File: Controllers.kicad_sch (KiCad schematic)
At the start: 5 parts

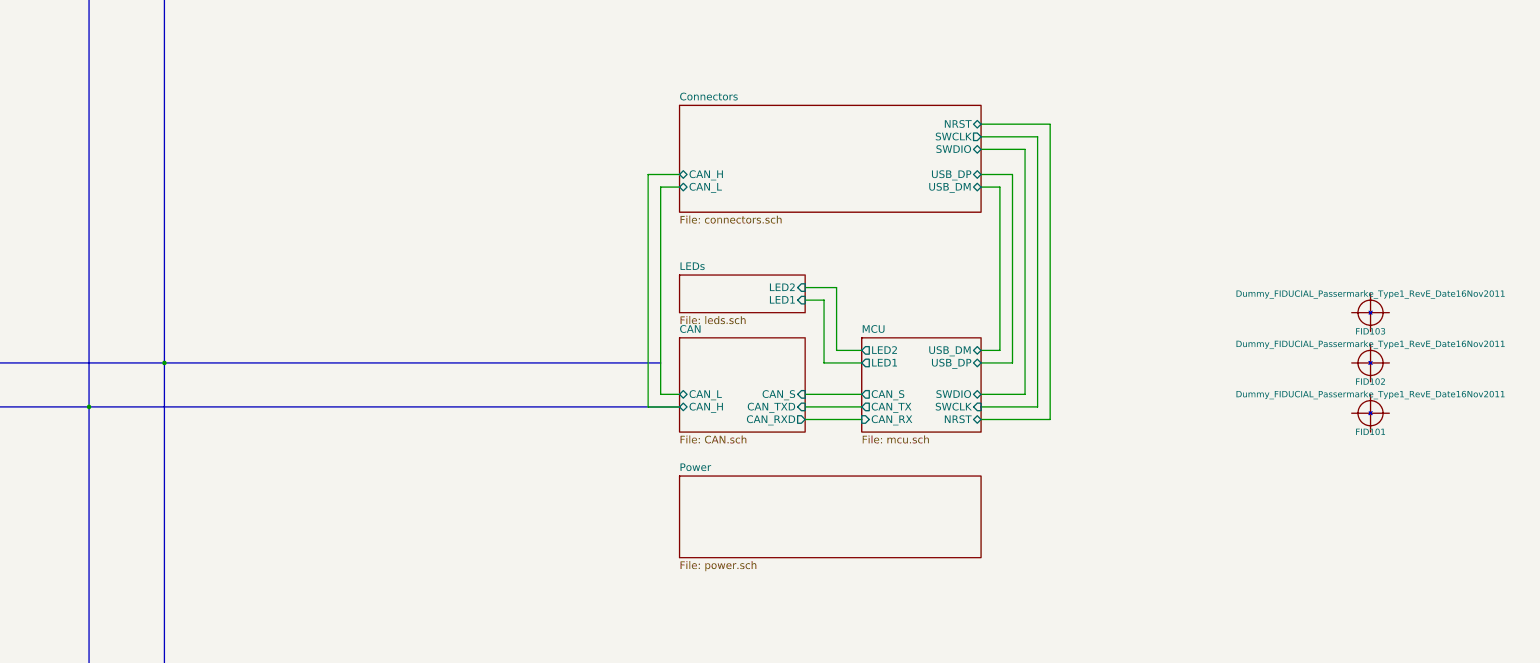
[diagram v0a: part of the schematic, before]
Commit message: Добавлен USB
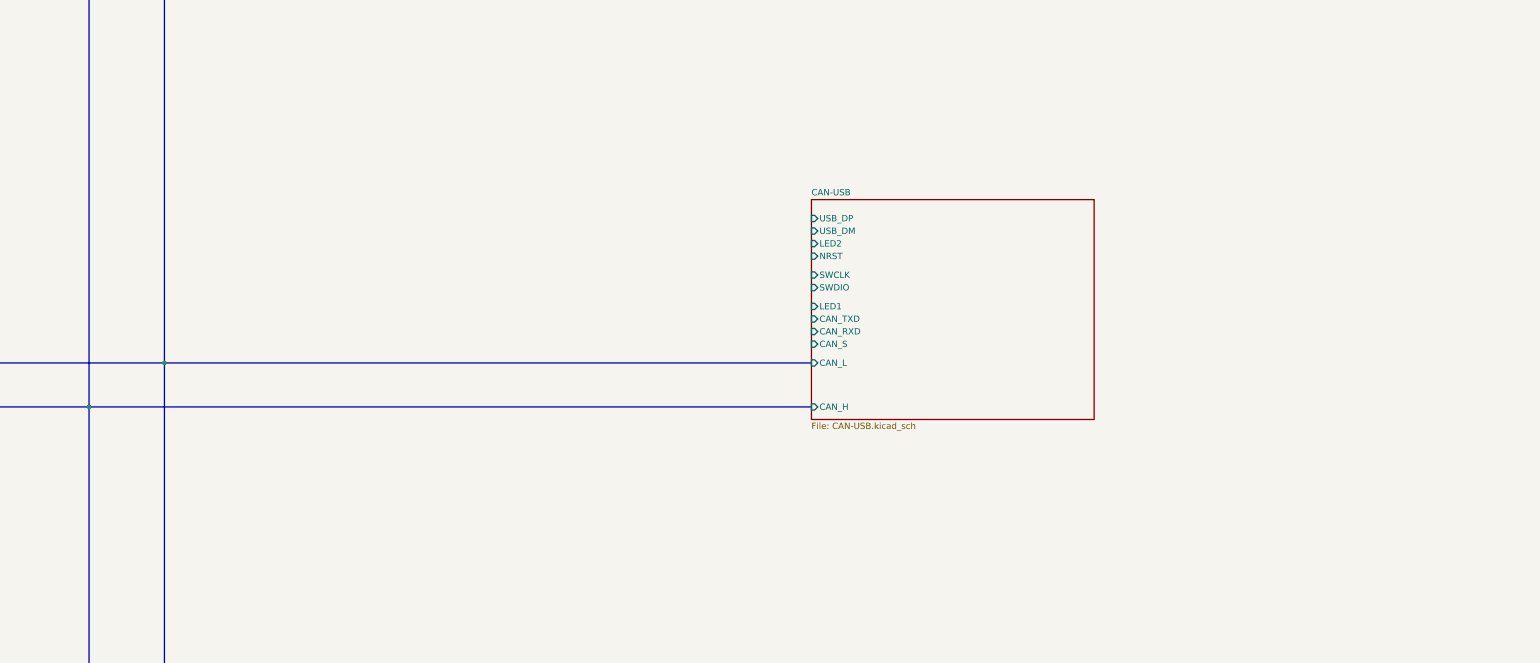
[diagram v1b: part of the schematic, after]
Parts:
- removed FID101, FID102, FID103: Dummy_FIDUCIAL_Passermarke_Type1_RevE_Date16Nov20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, Fiducials:Fiducial_1mm_Dia_2.54mm_Outer_CopperTop, symbol candleLight-rescue:Dummy_FIDUCIAL_Passermarke_Type1_RevE_Date16Nov2011
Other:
- removed sheet CAN
- removed sheet Connectors
- removed sheet LEDs
- removed sheet MCU
- removed sheet Power
- added sheet CAN-USB (CAN-USB.kicad_sch)
